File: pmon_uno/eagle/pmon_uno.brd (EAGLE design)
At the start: 50 x 50 mm, 42 parts, among them J1 USB, J2 USB, J3 TERMINAL-2, Q1 16Mhz, U1 LTC2943, U2 FT232RL, U3 LT1764AEQ, U4 ATMEGA328TQFP32

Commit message: Rearanged the leds pin to have a PWM option for the Status led.
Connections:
- removed net DEBUG_LED: R11.2, U4.14
- new net STATUS_LED: R11.2, U4.1
- net ACTIVITY_LED: now also U4.13; no longer U4.12
- net ERROR_LED: now also U4.12; no longer U4.13
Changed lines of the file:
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@@
 <signal name="ERROR_LED">
 <contactref element="R9" pad="2"/>
-<contactref element="U4" pad="13"/>
-<wire x1="9.74" y1="8.255" x2="22.625" y2="15.3924" width="0" layer="19" extent="1-1"/>
+<contactref element="U4" pad="12"/>
+<wire x1="9.74" y1="8.255" x2="21.825" y2="15.3924" width="0" layer="19" extent="1-1"/>
 </signal>
 <signal name="RESET">
@@
 <signal name="ACTIVITY_LED">
 <contactref element="R10" pad="2"/>
-<contactref element="U4" pad="12"/>
-<wire x1="14.82" y1="8.255" x2="21.825" y2="15.3924" width="0" layer="19" extent="1-1"/>
+<contactref element="U4" pad="13"/>
+<wire x1="14.82" y1="8.255" x2="22.625" y2="15.3924" width="0" layer="19" extent="1-1"/>
 </signal>
 <signal name="N$9">
@@
 <wire x1="19.05" y1="5.969" x2="19.05" y2="5.867" width="0.2032" layer="1"/>
 </signal>
-<signal name="DEBUG_LED">
+<signal name="STATUS_LED">
 <contactref element="R11" pad="2"/>
-<contactref element="U4" pad="14"/>
-<wire x1="19.9" y1="8.255" x2="23.425" y2="15.3924" width="0" layer="19" extent="1-1"/>
+<contactref element="U4" pad="1"/>
+<wire x1="19.9" y1="8.255" x2="17.9324" y2="22.485" width="0" layer="19" extent="1-1"/>
 </signal>
 <signal name="N$22">

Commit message: Layout completed.
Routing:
- net MISO: track 0.00 -> 56.5 mm
- net CONFIG2: track 0.00 -> 38.9 mm, vias 0 -> 1
- net SCK: track 0.00 -> 36.8 mm, vias 0 -> 1
- net MOSI: track 0.06 -> 32.1 mm
- net CONFIG3: track 0.00 -> 29.0 mm, vias 0 -> 1
- net CONFIG4: track 0.00 -> 27.4 mm, vias 0 -> 1
- net ACTION: track 0.16 -> 23.9 mm, vias 0 -> 2
- net +5V: track 55.5 -> 78.8 mm
- net RESET: track 0.81 -> 24.1 mm, vias 0 -> 1
- net STATUS_LED: track 0.00 -> 22.5 mm, vias 0 -> 2
- net SER_RX: track 0.18 -> 20.7 mm, vias 0 -> 4
- net CONFIG1: track 0.00 -> 20.5 mm, vias 0 -> 2
- net I2C-CLK: track 0.10 -> 19.6 mm, vias 0 -> 3
- net I2C-DATA: track 0.00 -> 18.7 mm, vias 0 -> 2
- net ERROR_LED: track 0.00 -> 15.4 mm
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
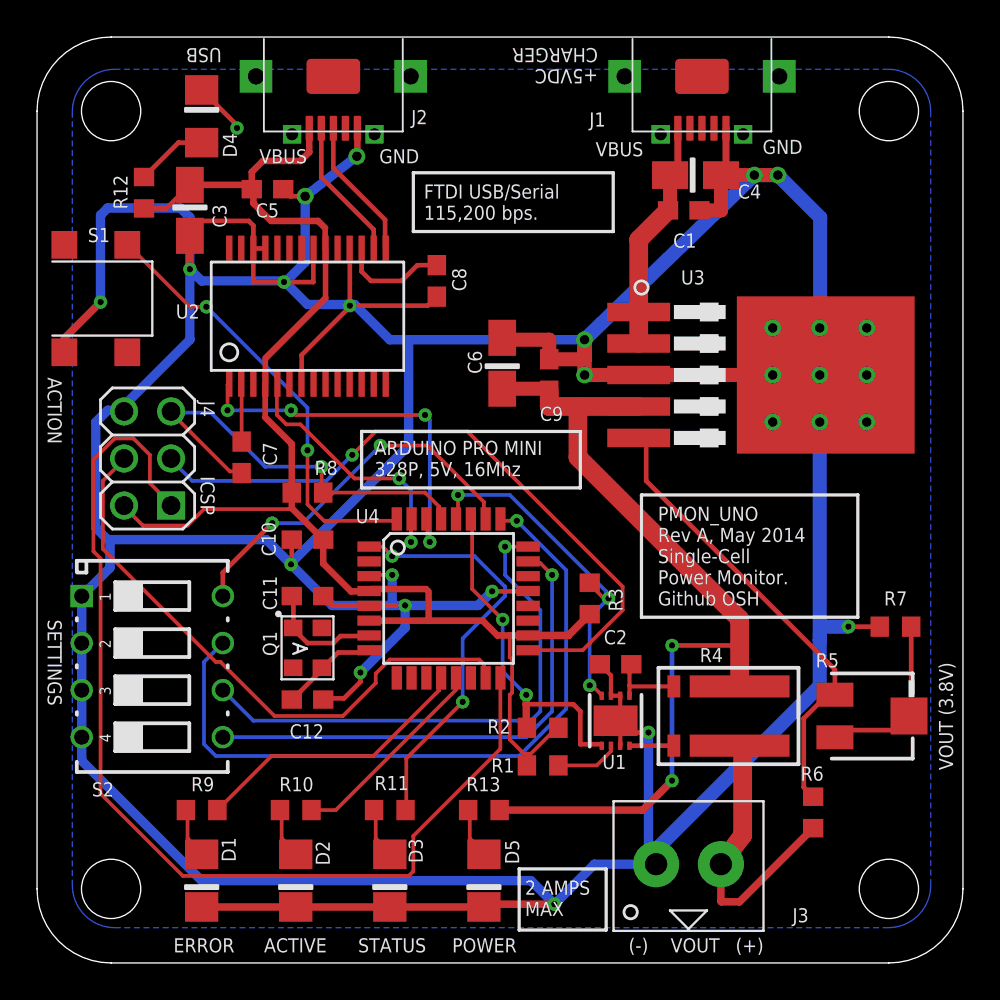
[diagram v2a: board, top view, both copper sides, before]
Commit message: Changed the button and power terminals to be top access (incremented to Rev B), Yet to be auto routed.
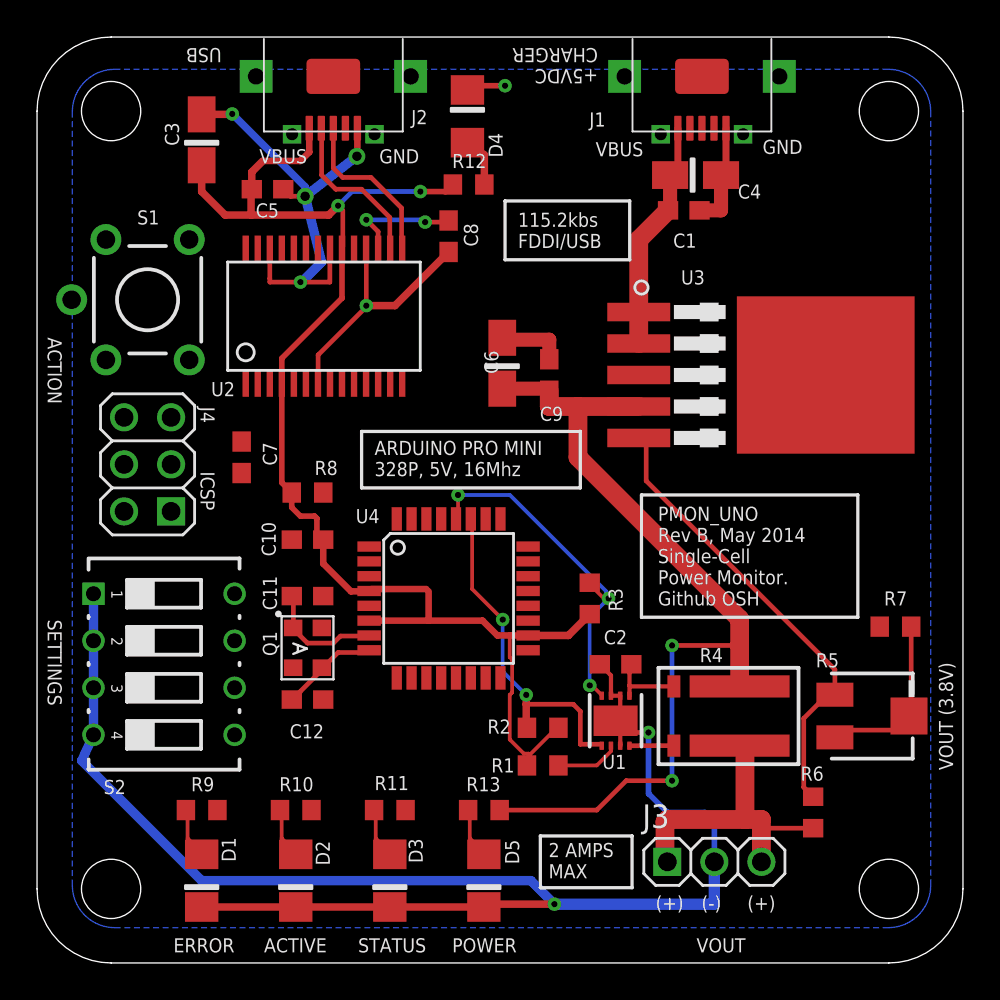
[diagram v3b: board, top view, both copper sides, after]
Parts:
- J3: value TERMINAL-2 -> (none); device pmon_uno:TERMINAL-2 -> pmon_uno:1X03
- S1: value PUSH_BUTTONEVQPSL -> PUSH_BUTTON_SHIELDED; device pmon_uno:EVQPSL-PUSH-BUTTON -> pmon_uno:TLE1105
- moved R12 17.5 mm to (23.3, 42.0), turned to 0 degrees
- moved D4 14.4 mm to (23.2, 45.7)
- moved C3 3.86 mm to (8.89, 44.5), turned to 270 degrees
- moved S1 2.79 mm to (5.97, 35.8), turned to 0 degrees
- moved C8 2.50 mm to (22.2, 39.2)
- moved J3 1.40 mm to (36.6, 5.46)
- moved U2 0.89 mm to (15.5, 34.9)
- moved S2 0.65 mm to (3.05, 19.9)
- moved J4 0.32 mm to (5.97, 26.9)
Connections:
- net ACTION: now also S1.B; no longer S1.1
- net GND: now also J3.2, S1.A, S1.G; no longer J3.1, S1.2
- net N$22: now also J3.1, J3.3; no longer J3.2
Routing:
- net GND: track 356.5 -> 140.0 mm, vias 28 -> 8
- net MISO: track 56.5 -> 0.00 mm
- net CONFIG2: track 38.9 -> 0.00 mm, vias 1 -> 0
- net SCK: track 36.8 -> 0.00 mm, vias 1 -> 0
- net MOSI: track 32.1 -> 0.00 mm
- net CONFIG3: track 29.0 -> 0.00 mm, vias 1 -> 0
- net CONFIG4: track 27.4 -> 0.00 mm, vias 1 -> 0
- net RESET: track 24.1 -> 0.09 mm, vias 1 -> 0
- net ACTION: track 23.9 -> 0.16 mm, vias 2 -> 0
- net STATUS_LED: track 22.5 -> 0.00 mm, vias 2 -> 0
- net CONFIG1: track 20.5 -> 0.00 mm, vias 2 -> 0
- net SER_RX: track 20.7 -> 0.30 mm, vias 4 -> 0
- net ERROR_LED: track 15.4 -> 0.00 mm
- net SER_TX: track 14.7 -> 0.14 mm, vias 2 -> 0
- net ACTIVITY_LED: track 11.1 -> 0.00 mm
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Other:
- board text added: "115.2kbs FDDI/USB"
- board text added: "PMON_UNO Rev B, May 2014 Single-Cell Power Monitor. Github OSH"
- board text removed: "FTDI USB/Serial 115,200 bps."
- board text removed: "PMON_UNO Rev A, May 2014 Single-Cell Power Monitor. Github OSH"

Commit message: Rev B is fully routed.
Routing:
- net GND: track 140.0 -> 289.5 mm, vias 8 -> 25
- net MISO: track 0.00 -> 58.0 mm
- net SCK: track 0.00 -> 36.6 mm, vias 0 -> 1
- net MOSI: track 0.00 -> 35.8 mm
- net CONFIG4: track 0.00 -> 23.8 mm, vias 0 -> 1
- net CONFIG3: track 0.00 -> 20.9 mm, vias 0 -> 2
- net ACTION: track 0.16 -> 20.8 mm, vias 0 -> 2
- net CONFIG2: track 0.00 -> 20.0 mm, vias 0 -> 1
- net STATUS_LED: track 0.00 -> 18.7 mm, vias 0 -> 2
- net RESET: track 0.09 -> 18.3 mm, vias 0 -> 2
- net CONFIG1: track 0.00 -> 17.9 mm, vias 0 -> 1
- net SER_RX: track 0.30 -> 18.0 mm, vias 0 -> 2
- net ERROR_LED: track 0.00 -> 15.4 mm
- net SER_TX: track 0.14 -> 12.2 mm, vias 0 -> 2
- net +5V: track 76.7 -> 88.0 mm
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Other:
- board text added: "ERRORS"
- board text removed: "ERROR"
- board text removed: "POWER"
